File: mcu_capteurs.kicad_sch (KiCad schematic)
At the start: 70 parts, among them J15 BOOT0, J4 STLINK, SW1 435431019840, U2 TCA9517DR, U3 WSEN-PDUS, U4 STM32G474CEUx, Y1 16 MHz

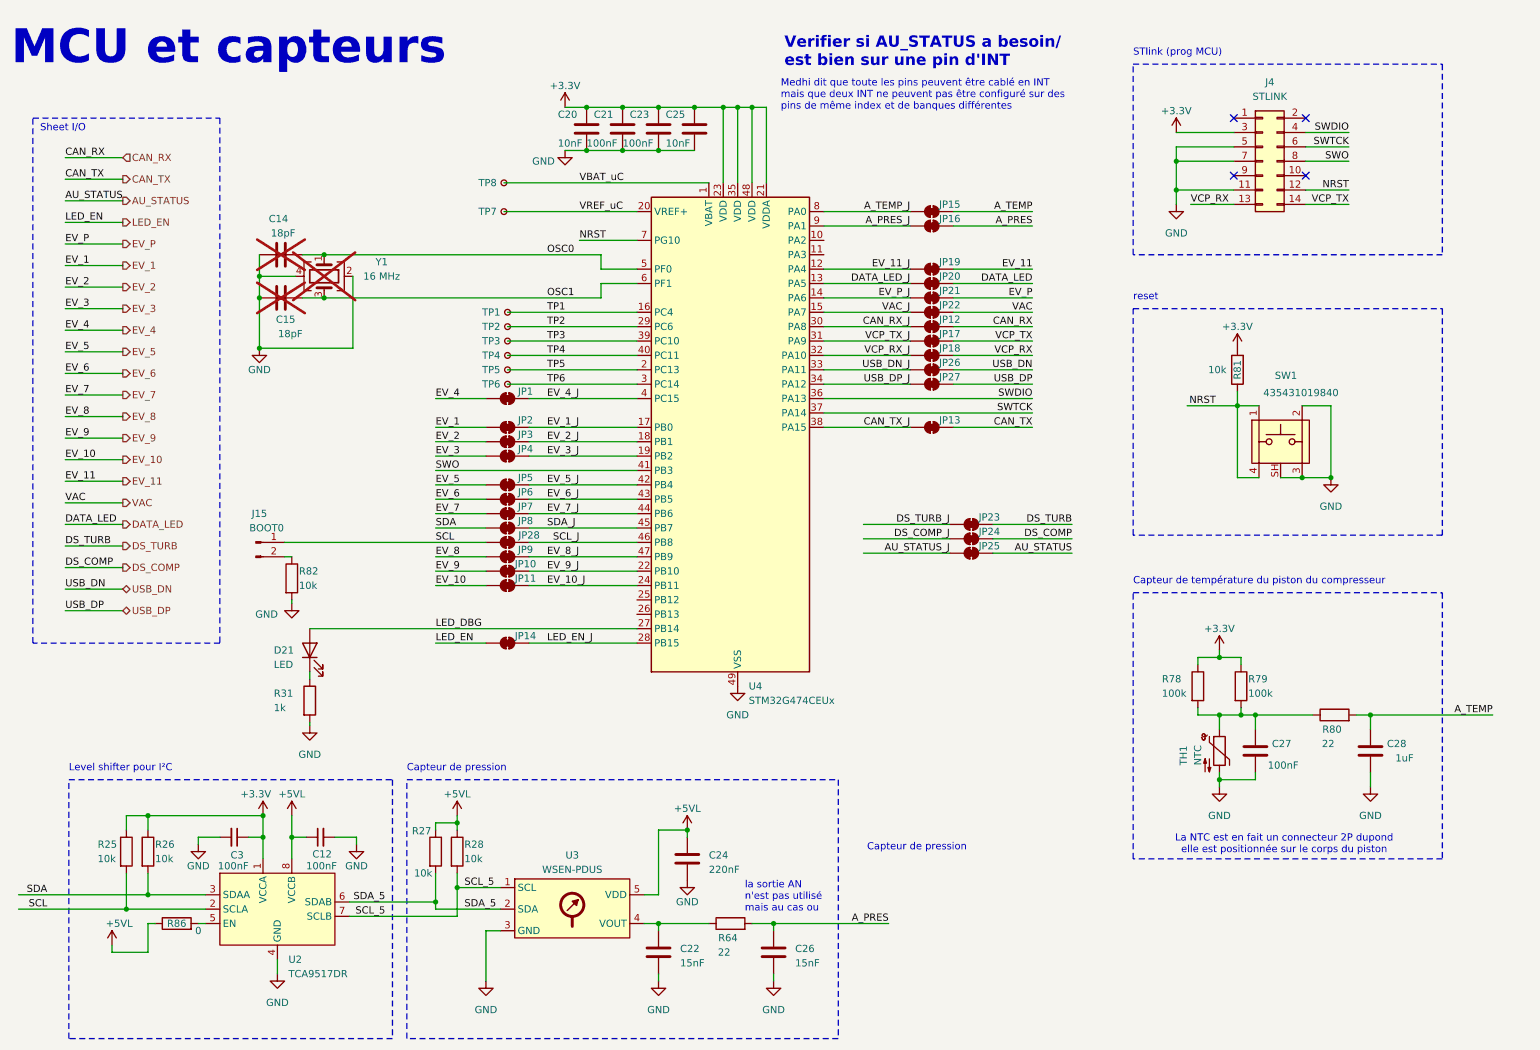
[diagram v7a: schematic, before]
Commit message: fin du placement et reassignation des pins uC
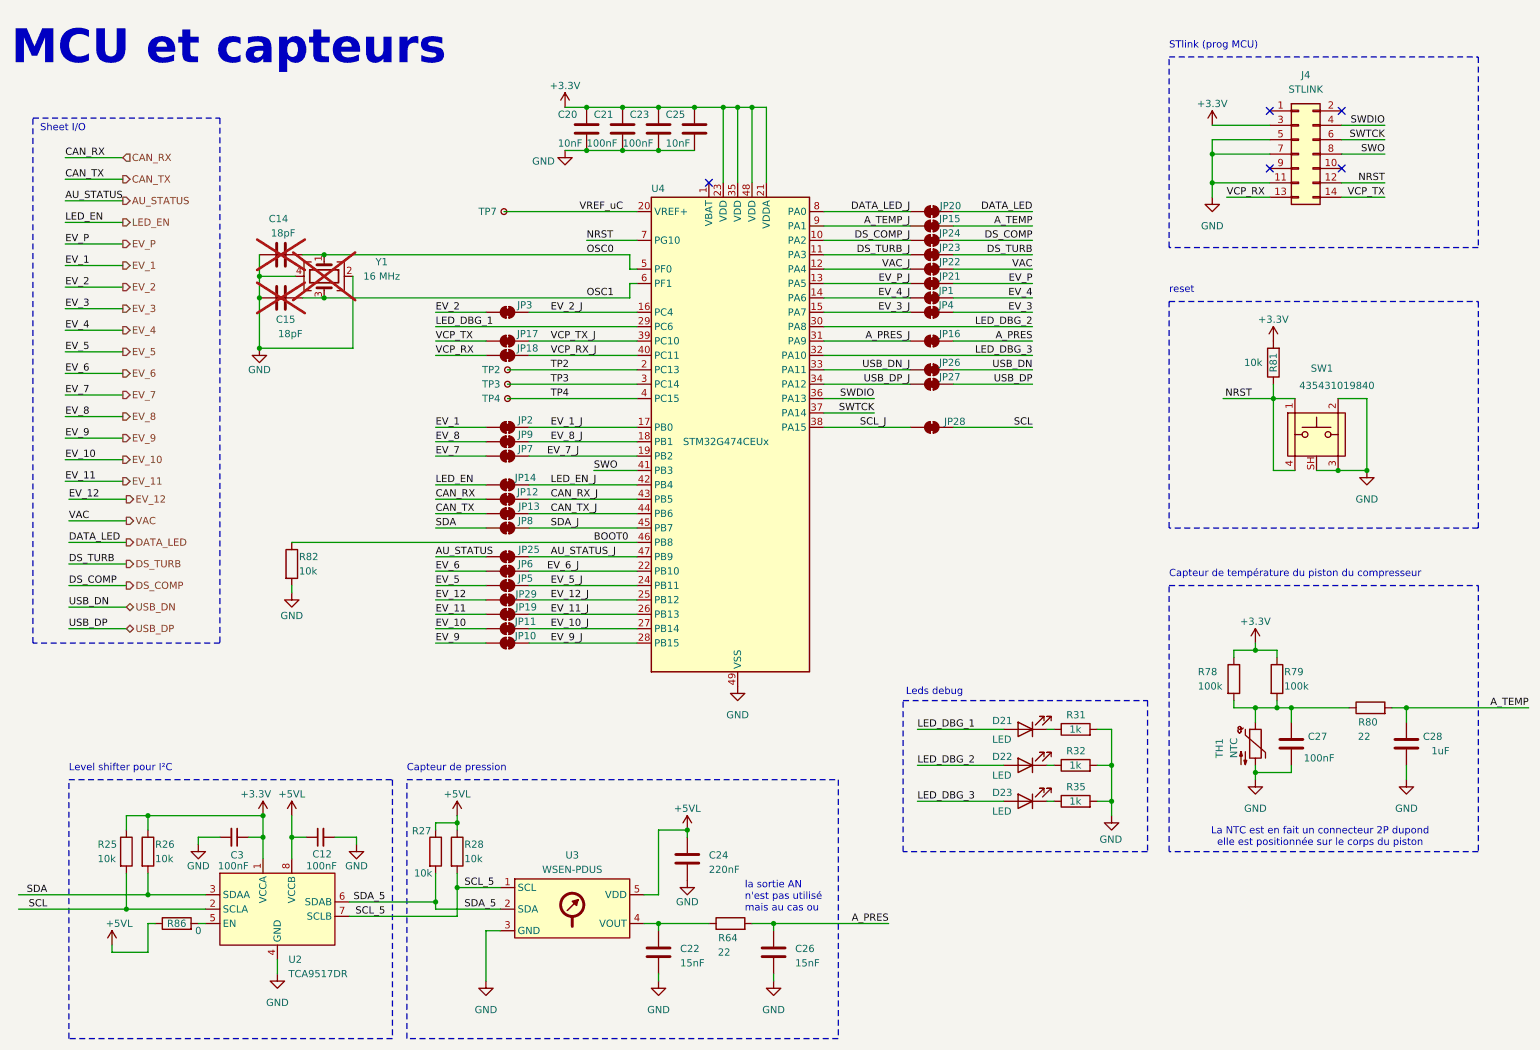
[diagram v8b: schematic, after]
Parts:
- removed J15: BOOT0, Connector_PinHeader_2.54mm:PinHeader_1x02_P2.54mm_Vertical, symbol Connector:Conn_01x02_Pin
- removed TP1, TP5, TP6, TP8: TestPoint_Small, TestPoint:TestPoint_Pad_D1.0mm, symbol Connector:TestPoint_Small
- added D22, D23: LED, LED_SMD:LED_0603_1608Metric, symbol Device:LED
- added JP29: SolderJumper_2_Bridged, 12V-actuators_pcb:R_0402_1005Metric_jumperClosed, symbol Jumper:SolderJumper_2_Bridged
- added R32, R35: 1k, Resistor_SMD:R_0603_1608Metric, symbol Device:R
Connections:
- net TP1 is gone; now on net EV_2_J: U4.16 (PC4)
- net TP5 is gone; now on net TP2: U4.2 (PC13)
- net TP6 is gone; now on net TP3: U4.3 (PC14)
- net AU_STATUS_J: now also U4.47 (PB9)
- net A_PRES_J: now also U4.31 (PA9); no longer U4.9 (PA1)
- net A_TEMP_J: now also U4.9 (PA1); no longer U4.8 (PA0)
- net CAN_RX_J: now also U4.43 (PB5); no longer U4.30 (PA8)
- net CAN_TX_J: now also U4.44 (PB6); no longer U4.38 (PA15)
- net DATA_LED_J: now also U4.8 (PA0); no longer U4.13 (PA5)
- net DS_COMP_J: now also U4.10 (PA2)
- net DS_TURB_J: now also U4.11 (PA3)
- net EV_10_J: now also U4.27 (PB14); no longer U4.24 (PB11)
- net EV_11_J: now also U4.26 (PB13); no longer U4.12 (PA4)
- net EV_2_J: no longer U4.18 (PB1)
- net EV_3_J: now also U4.15 (PA7); no longer U4.19 (PB2)
- net EV_4_J: now also U4.14 (PA6); no longer U4.4 (PC15)
- net EV_5_J: now also U4.24 (PB11); no longer U4.42 (PB4)
- net EV_6_J: now also U4.22 (PB10); no longer U4.43 (PB5)
- net EV_7_J: now also U4.19 (PB2); no longer U4.44 (PB6)
- net EV_8_J: now also U4.18 (PB1); no longer U4.47 (PB9)
- net EV_9_J: now also U4.28 (PB15); no longer U4.22 (PB10)
- net EV_P_J: now also U4.13 (PA5); no longer U4.14 (PA6)
- net GND: now also R32.2, R35.2
- net LED_EN_J: now also U4.42 (PB4); no longer U4.28 (PB15)
- net SCL_J: now also U4.38 (PA15); no longer U4.46 (PB8)
- net TP2: no longer U4.29 (PC6)
- net TP3: no longer U4.39 (PC10)
- net TP4: now also U4.4 (PC15); no longer U4.40 (PC11)
- net VAC_J: now also U4.12 (PA4); no longer U4.15 (PA7)
- net VCP_RX_J: now also U4.40 (PC11); no longer U4.32 (PA10)
- net VCP_TX_J: now also U4.39 (PC10); no longer U4.31 (PA9)
- net BOOT0: now reaches R82.1
- net BOOT0: now also U4.46 (PB8)
- net EV_12_J: now reaches U4.25 (PB12)
- net EV_12_J: now also JP29.1 (A)
- net LED_DBG renamed LED_DBG_1
- net LED_DBG_1: now also U4.29 (PC6); no longer U4.27 (PB14)
- net VBAT_uC: no longer names the net of U4.1 (VBAT)
- new net: D22.1 (K), R32.1
- new net: D23.1 (K), R35.1
- new net EV_12: JP29.2 (B)
- new net LED_DBG_2: D22.2 (A), U4.30 (PA8)
- new net LED_DBG_3: D23.2 (A), U4.32 (PA10)
- no-connect marks 4 -> 5
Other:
- note added: "Leds debug"
- note removed: "Medhi dit que toute les pins peuvent être cablé en INT mais que deux INT ne peuvent pas être configuré sur des pins de même index et de banques différentes"
- note removed: "Verifier si AU_STATUS a besoin/ est bien sur une pin d'INT"
- moved on the sheet: C27, C28, D21, J4, JP1, JP10, JP11, JP12, JP13, JP14, JP15, JP16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
